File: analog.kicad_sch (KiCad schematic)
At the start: 28 parts, among them U2 AD9833xRM, U4 LM4881M

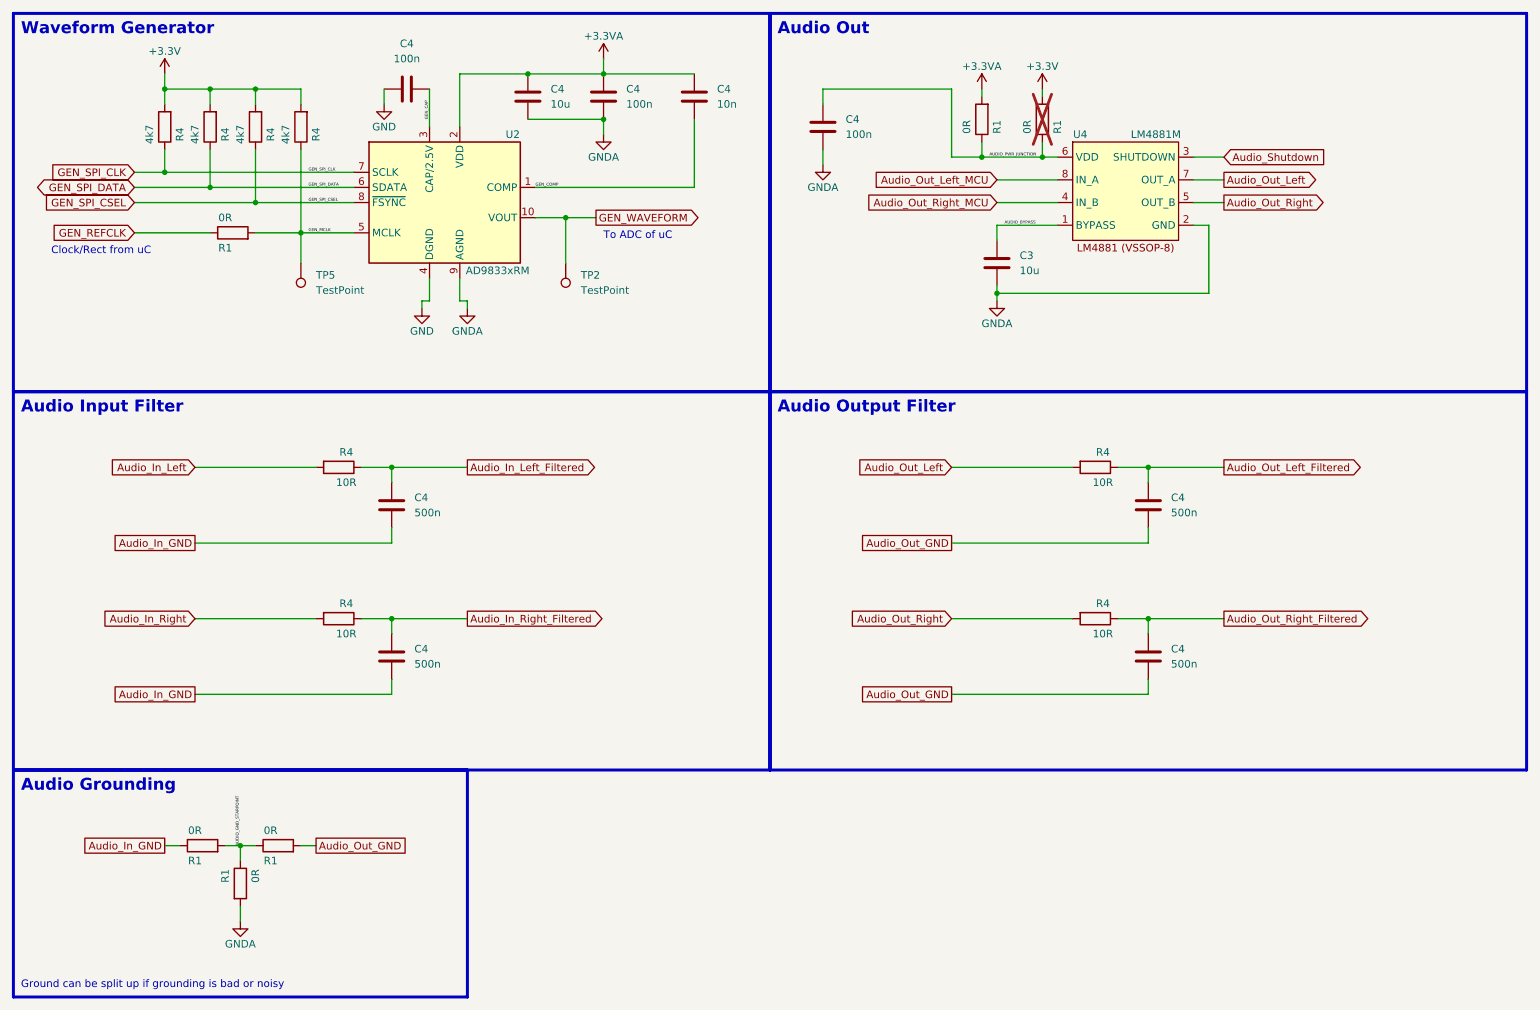
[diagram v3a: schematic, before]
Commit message: Layout and routing basically done, check again before delivering
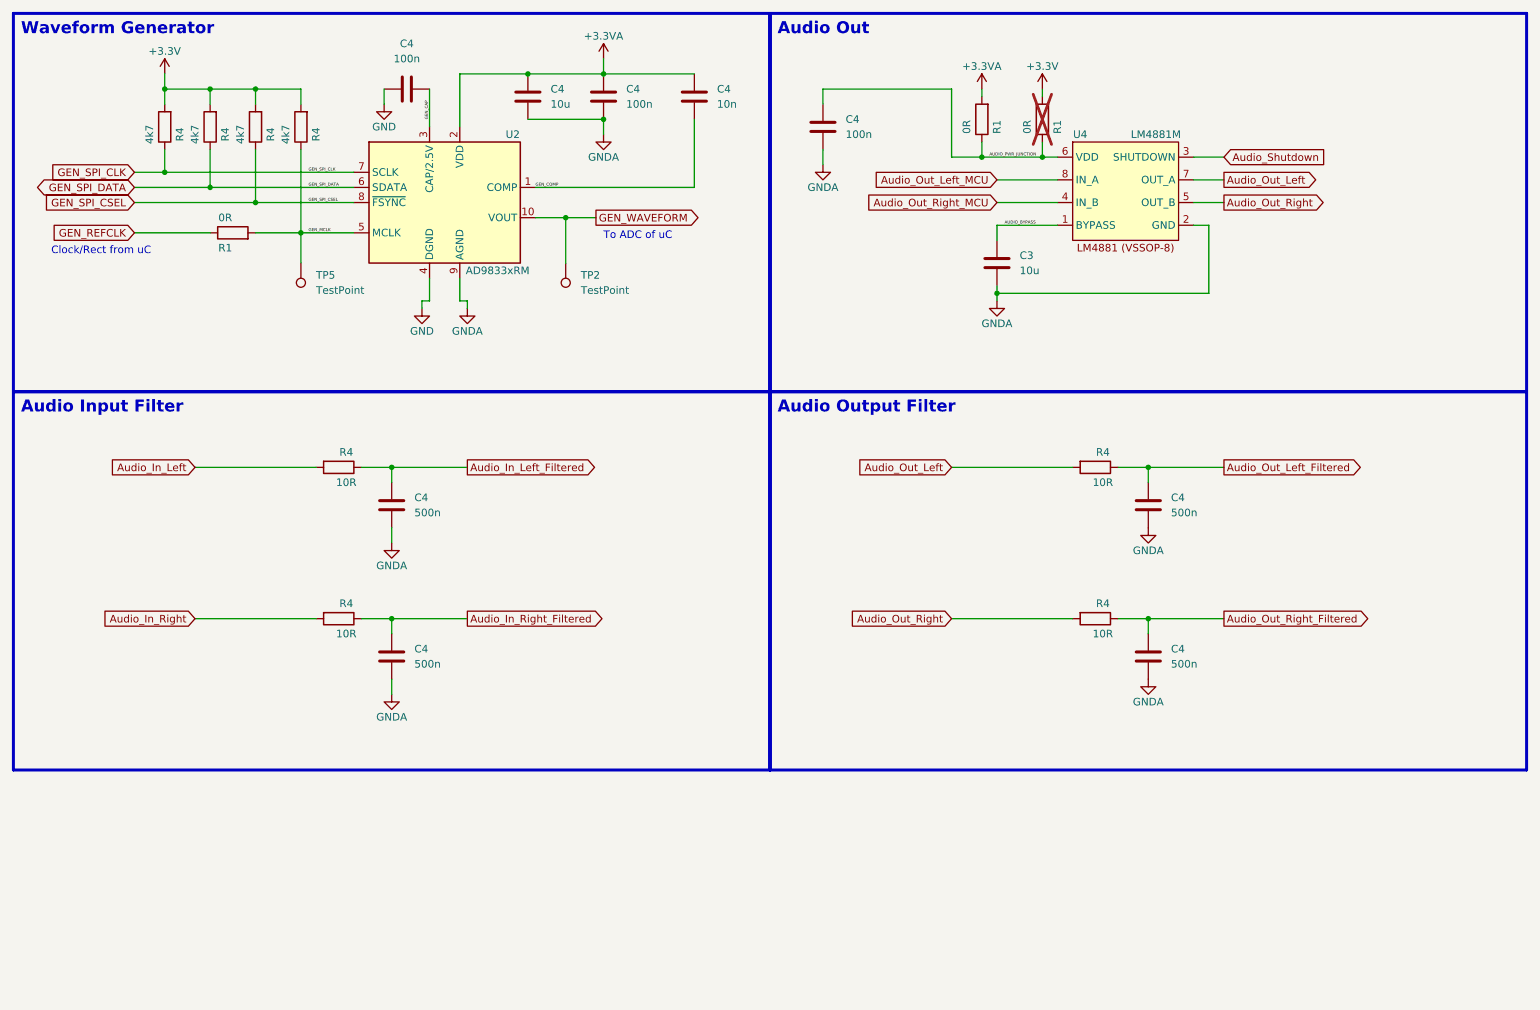
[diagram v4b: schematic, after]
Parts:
- removed R1 (x3): 0R, Resistor_SMD:R_0805_2012Metric, symbol Device:R
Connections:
- net Audio_In_GND is gone; now on net GNDA: C4.2, C4.2
- net Audio_Out_GND is gone; now on net GNDA: C4.2, C4.2
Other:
- note removed: "Audio Grounding"
- note removed: "Ground can be split up if grounding is bad or noisy"

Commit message: Added capacitor voltage rating
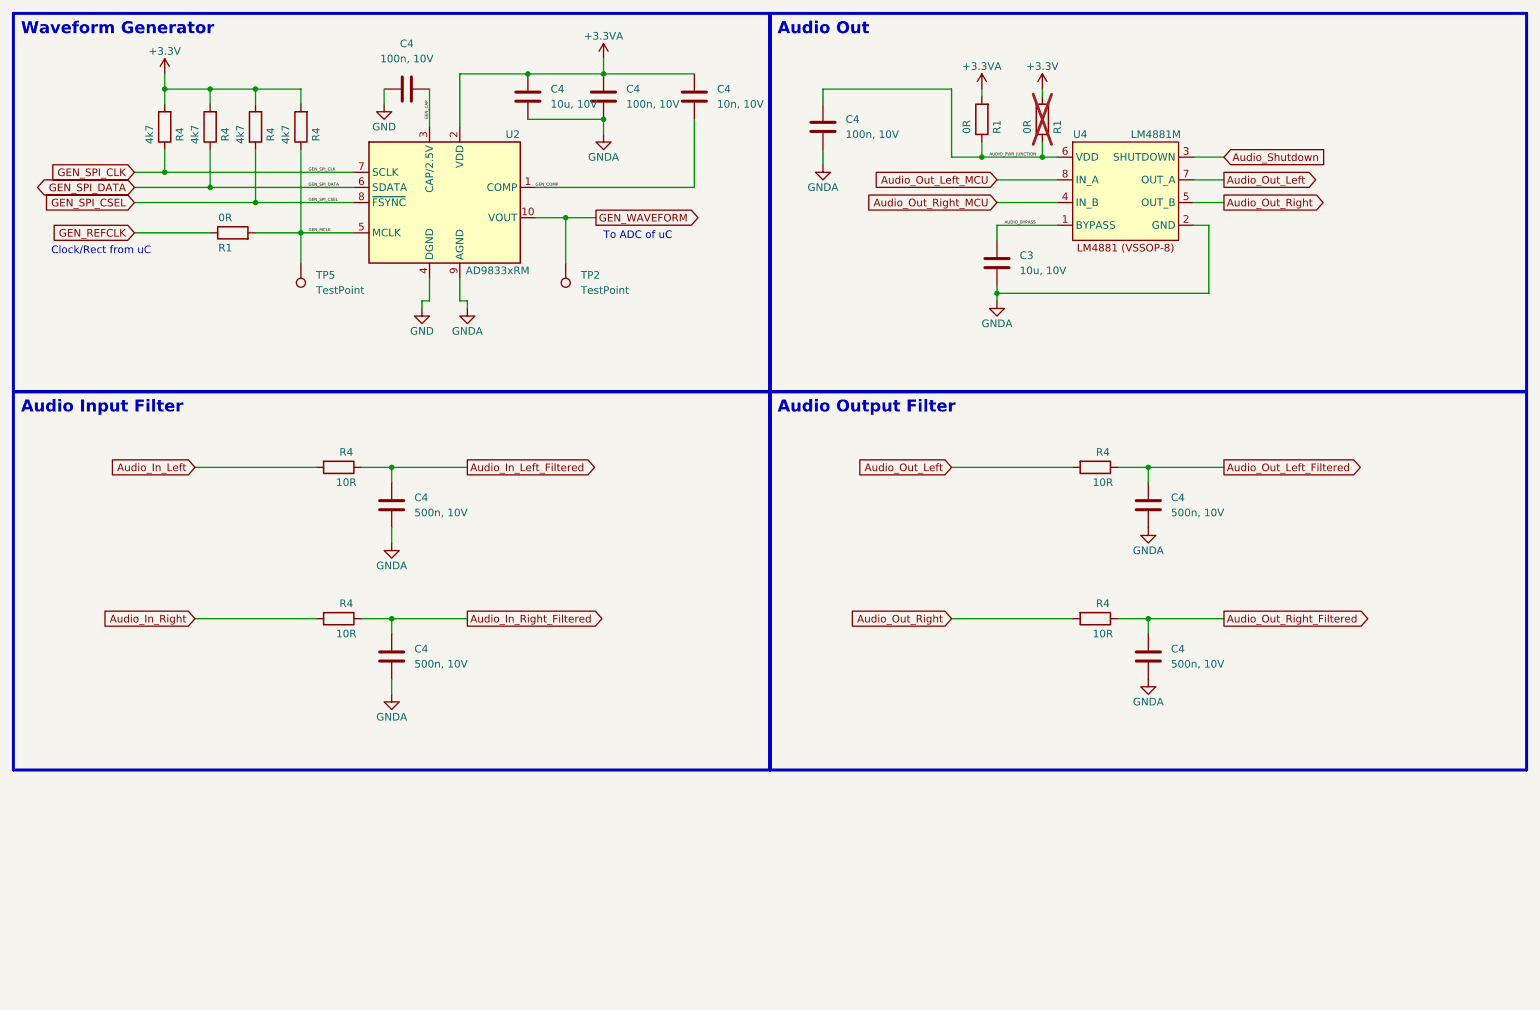
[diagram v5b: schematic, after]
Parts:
- C3, C4: value 10u -> 10u, 10V
- C4: value 500n -> 500n, 10V
- C4: value 100n -> 100n, 10V
- C4: value 10n -> 10n, 10V
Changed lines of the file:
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@@
       (effects (font (size 1.27 1.27)) (justify left))
     )
-    (property "Value" "500n" (at 219.71 109.22 0)
+    (property "Value" "500n, 10V" (at 219.71 109.22 0)
       (effects (font (size 1.27 1.27)) (justify left))
     )
@@
       (effects (font (size 1.27 1.27)) (justify left))
     )
-    (property "Value" "500n" (at 219.71 134.62 0)
+    (property "Value" "500n, 10V" (at 219.71 134.62 0)
       (effects (font (size 1.27 1.27)) (justify left))
     )
@@
       (effects (font (size 1.27 1.27)) (justify left))
     )
-    (property "Value" "10u" (at 115.57 40.64 0)
+    (property "Value" "10u, 10V" (at 115.57 40.64 0)
       (effects (font (size 1.27 1.27)) (justify left))
     )
@@
       (effects (font (size 1.27 1.27)) (justify left))
     )
-    (property "Value" "100n" (at 128.27 40.64 0)
+    (property "Value" "100n, 10V" (at 128.27 40.64 0)
       (effects (font (size 1.27 1.27)) (justify left))
     )
@@
       (effects (font (size 1.27 1.27)) (justify left))
     )
-    (property "Value" "10u" (at 194.31 68.58 0)
+    (property "Value" "10u, 10V" (at 194.31 68.58 0)
       (effects (font (size 1.27 1.27)) (justify left))
     )
@@
       (effects (font (size 1.27 1.27)) (justify left))
     )
-    (property "Value" "500n" (at 92.71 109.22 0)
+    (property "Value" "500n, 10V" (at 92.71 109.22 0)
       (effects (font (size 1.27 1.27)) (justify left))
     )
@@
       (effects (font (size 1.27 1.27)) (justify left))
     )
-    (property "Value" "500n" (at 92.71 134.62 0)
+    (property "Value" "500n, 10V" (at 92.71 134.62 0)
       (effects (font (size 1.27 1.27)) (justify left))
     )
@@
       (effects (font (size 1.27 1.27)) (justify left))
     )
-    (property "Value" "10n" (at 143.51 40.64 0)
+    (property "Value" "10n, 10V" (at 143.51 40.64 0)
       (effects (font (size 1.27 1.27)) (justify left))
     )
@@
       (effects (font (size 1.27 1.27)))
     )
-    (property "Value" "100n" (at 91.44 33.02 90)
+    (property "Value" "100n, 10V" (at 91.44 33.02 90)
       (effects (font (size 1.27 1.27)))
     )
@@
       (effects (font (size 1.27 1.27)) (justify left))
     )
-    (property "Value" "100n" (at 165.1 45.72 0)
-      (effects (font (size 1.27 1.27)) (justify left))
-    )
+    (property "Value" "100n, 10V" (at 165.1 45.72 0)
+      (effects (font (size 1.27 1.27)) (justify left))
+    )
